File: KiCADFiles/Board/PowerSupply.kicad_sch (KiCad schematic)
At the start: 30 parts, among them J3 Barrel_Jack_PTH, U2 LT1962-3.3, U3 LT1962-5, U8 LT1962

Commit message: chose all components
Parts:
- removed C7: 47uF, ~, symbol SuperAudioBoard-rescue:CP1
- added C7: 100u, Capacitor_THT:CP_Radial_D5.0mm_P2.00mm, symbol Device:C_Small_US
- C1, C10, C11, C12, C13, C16, C17, C2, C3, C4, C8: value 10uF -> 10u; footprint ~ -> PCM_SparkFun-Capacitor:C_0805_2012Metric; MPN (none) -> CL21A106KAYNNNG; Voltage (none) -> 25V
- C5, C6: footprint ~ -> PCM_SparkFun-Capacitor:C_0603_1608Metric; MPN (none) -> C0603C103K5RACTU
- D1, D2: footprint ~ -> LED_SMD:LED_0805_2012Metric; MPN (none) -> 599-0110-137F
- FB1, FB2: value 330R -> 330; footprint ~ -> Inductor_SMD:L_0805_2012Metric; MPN (none) -> MPZ2012S331ATD25
- L2, L3: value 5.2uH -> 6.8uH; footprint ~ -> Inductor_SMD:L_0805_2012Metric; MPN (none) -> MLZ2012N6R8LT000
- R1: value 270 -> 3.3k; footprint ~ -> PCM_SparkFun-Resistor:R_0805_2012Metric; MPN (none) -> ERA-6AEB332V
- R2: value 620 -> 3.3k; footprint ~ -> PCM_SparkFun-Resistor:R_0805_2012Metric; MPN (none) -> ERA-6AEB332V
- R3: footprint (none) -> PCM_SparkFun-Resistor:R_0805_2012Metric; MPN (none) -> ERA-6AEB3922V; Tol (none) -> 1%
- R4: footprint (none) -> PCM_SparkFun-Resistor:R_0805_2012Metric; MPN (none) -> ERA-6AEB332V; Tol (none) -> 1%
- TP1, TP2: footprint (none) -> TestPoint:TestPoint_2Pads_Pitch2.54mm_Drill0.8mm; now not fitted
- U2: footprint (none) -> Package_SO:MSOP-8_3x3mm_P0.65mm; MPN (none) -> LT1962EMS8-3.3
- U3: footprint (none) -> Package_SO:MSOP-8_3x3mm_P0.65mm; MPN (none) -> LT1962EMS8-5
- U8: MPN (none) -> LT1962EMS8
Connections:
- net GND: now also C7.2
- net at C8.1, FB1.2, U8.5 (~{SHDN})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: now also C7.1

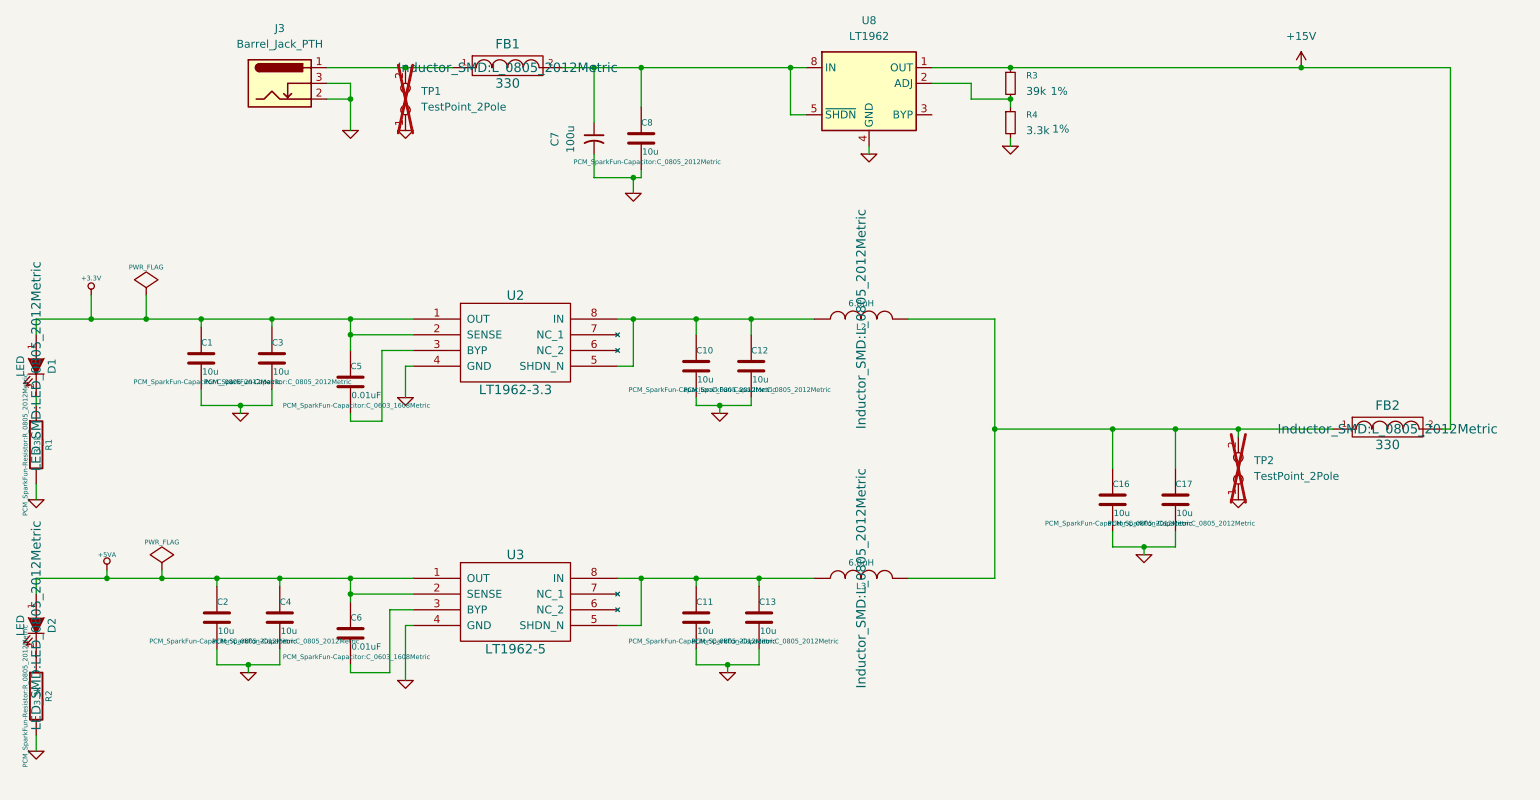
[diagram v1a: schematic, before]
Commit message: replaced sw with relay, routed line amp section
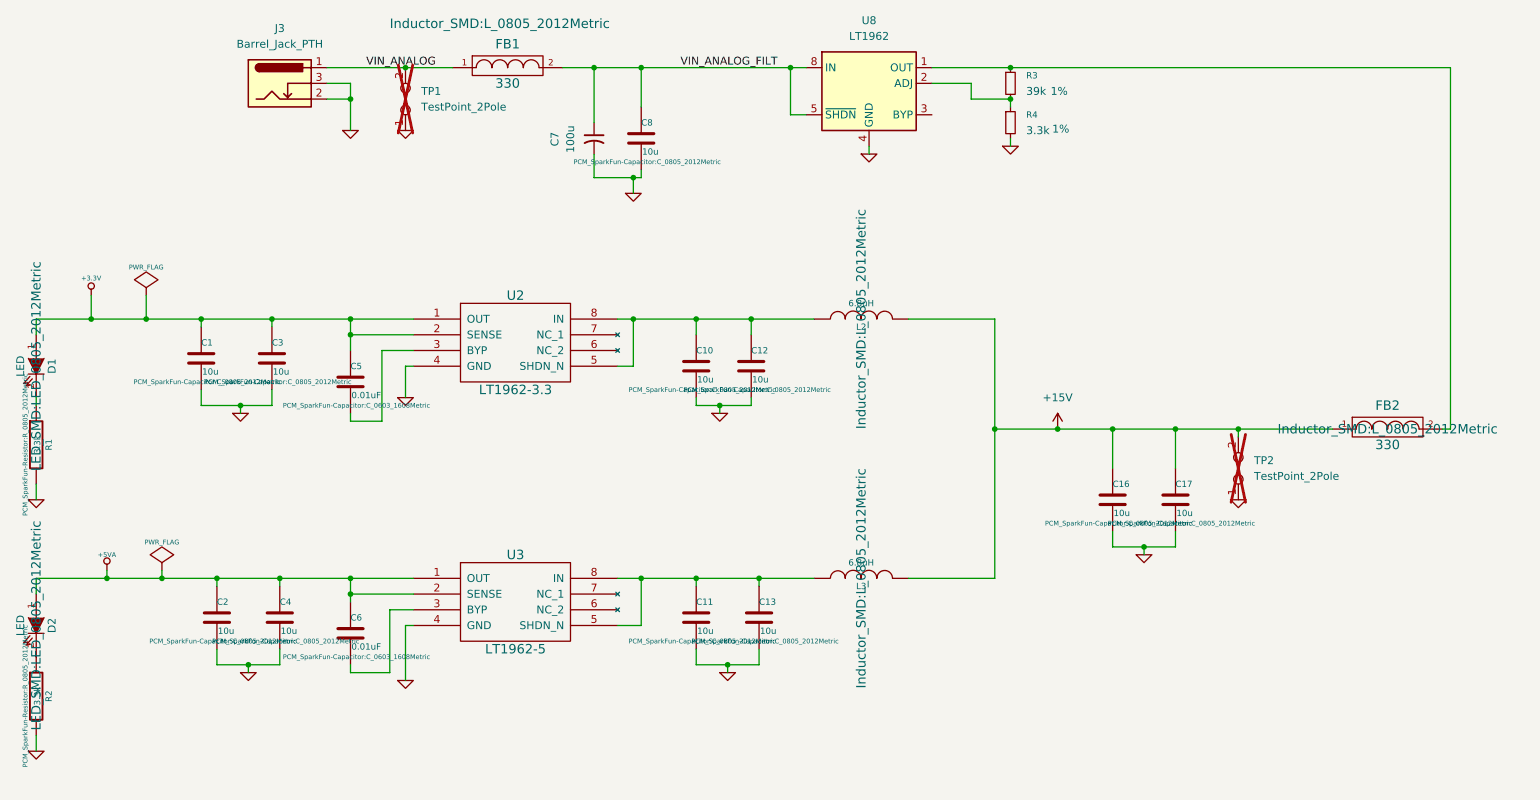
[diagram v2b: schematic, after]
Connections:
- net +15V: now also C16.1, C17.1, FB2.1, L2.2, L3.2, TP2.2; no longer FB2.2, R3.1, U8.1 (OUT)
- net VIN_ANALOG_FILT: now reaches C7.1, C8.1, FB1.2, U8.5 (~{SHDN}), U8.8 (IN)
- net VIN_ANALOG: now reaches FB1.1, J3.1 (PWR), TP1.2
- new net: FB2.2, R3.1, U8.1 (OUT)
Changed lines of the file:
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@@
 	)
 	(junction
-		(at 240.03 55.88)
-		(diameter 0)
-		(color 0 0 0 0)
-	)
-	(junction
 		(at 64.77 138.43)
 		(diameter 0)
@@
 	)
 	(junction
+		(at 200.66 114.3)
+		(diameter 0)
+		(color 0 0 0 0)
+	)
+	(junction
 		(at 74.93 138.43)
 		(diameter 0)
@@
 	(wire
 		(pts
-			(xy 240.03 55.88) (xy 264.16 55.88)
+			(xy 193.04 55.88) (xy 264.16 55.88)
 		)
 		(stroke
@@
 	(wire
 		(pts
-			(xy 193.04 55.88) (xy 240.03 55.88)
-		)
-		(stroke
-			(width 0)
-			(type default)
-		)
-	)
-	(wire
-		(pts
 			(xy 129.54 96.52) (xy 132.08 96.52)
 		)
@@
 	(wire
 		(pts
-			(xy 190.5 114.3) (xy 209.55 114.3)
+			(xy 190.5 114.3) (xy 200.66 114.3)
 		)
 		(stroke
@@
 	(wire
 		(pts
+			(xy 200.66 114.3) (xy 209.55 114.3)
+		)
+		(stroke
+			(width 0)
+			(type default)
+		)
+	)
+	(wire
+		(pts
 			(xy 62.23 97.79) (xy 62.23 96.52)
 		)
@@
 		)
 	)
+	(label "VIN_ANALOG"
+		(at 88.9 55.88 0)
+		(effects
+			(font
+				(size 1.27 1.27)
+			)
+			(justify left bottom)
+		)
+	)
+	(label "VIN_ANALOG_FILT"
+		(at 139.7 55.88 0)
+		(effects
+			(font
+				(size 1.27 1.27)
+			)
+			(justify left bottom)
+		)
+	)
 	(symbol
 		(lib_name "LT1962-3.3_2")
@@
 		(on_board yes)
 		(dnp no)
+		(fields_autoplaced yes)
 		(property "Reference" "#PWR010"
 			(at 132.08 76.2 0)
@@
 		(on_board yes)
 		(dnp no)
+		(fields_autoplaced yes)
 		(property "Reference" "C8"
 			(at 133.35 64.77 0)
@@
 		)
 		(property "Footprint" "Inductor_SMD:L_0805_2012Metric"
-			(at 111.76 55.88 0)
+			(at 110.49 48.768 0)
 			(effects
 				(font
@@
 	(symbol
 		(lib_id "power:+15V")
-		(at 240.03 55.88 0)
+		(at 200.66 114.3 0)
 		(unit 1)
 		(exclude_from_sim no)
@@
 		(fields_autoplaced yes)
 		(property "Reference" "#PWR012"
-			(at 240.03 59.69 0)
+			(at 200.66 118.11 0)
 			(effects
 				(font
@@
 		)
 		(property "Value" "+15V"
-			(at 240.03 50.8 0)
+			(at 200.66 109.22 0)
 			(effects
 				(font
@@
 		)
 		(property "Footprint" ""
-			(at 240.03 55.88 0)
+			(at 200.66 114.3 0)
 			(effects
 				(font
@@
 		)
 		(property "Datasheet" ""
-			(at 240.03 55.88 0)
+			(at 200.66 114.3 0)
 			(effects
 				(font
@@
 		)
 		(property "Description" "Power symbol creates a global label with name \"+15V\""
-			(at 240.03 55.88 0)
+			(at 200.66 114.3 0)
 			(effects
 				(font
@@
 		)
 		(instances
-			(project ""
+			(project "SuperAudioBoard"
 				(path "/01f65e03-4e05-4001-87b4-b3e88e4198ab/00000000-0000-0000-0000-000054459109"
 					(reference "#PWR012")
@@
 		(on_board yes)
 		(dnp no)
+		(fields_autoplaced yes)
 		(property "Reference" "R3"
 			(at 195.58 57.1499 0)
@@
 		(on_board yes)
 		(dnp no)
+		(fields_autoplaced yes)
 		(property "Reference" "C7"
 			(at 119.38 67.437 90)
@@
 		(on_board yes)
 		(dnp no)
+		(fields_autoplaced yes)
 		(property "Reference" "R4"
 			(at 195.58 63.4999 0)
@@
 		(on_board yes)
 		(dnp no)
+		(fields_autoplaced yes)
 		(property "Reference" "#PWR05"
 			(at 170.18 69.85 0)
@@
 		(on_board yes)
 		(dnp no)
+		(fields_autoplaced yes)
 		(property "Reference" "#PWR011"
 			(at 193.04 68.58 0)

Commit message: finished layout, passed DRC
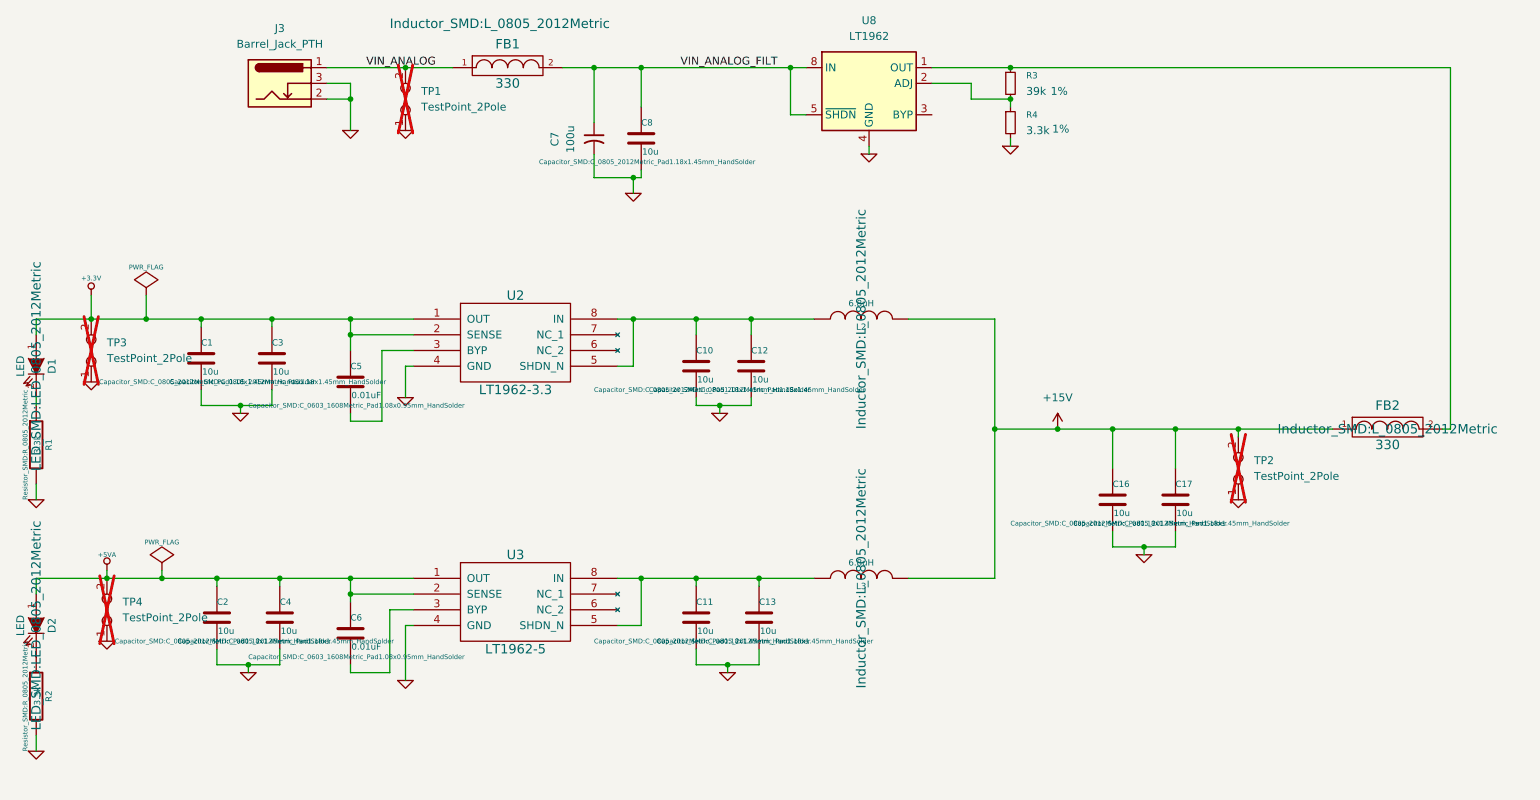
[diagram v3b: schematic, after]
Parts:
- added TP3, TP4: TestPoint_2Pole, TestPoint:TestPoint_2Pads_Pitch2.54mm_Drill0.8mm, symbol Connector:TestPoint_2Pole
- C1, C10, C11, C12, C13, C16, C17, C2, C3, C4, C8: footprint PCM_SparkFun-Capacitor:C_0805_2012Metric -> Capacitor_SMD:C_0805_2012Metric_Pad1.18x1.45mm_HandSolder
- C5, C6: footprint PCM_SparkFun-Capacitor:C_0603_1608Metric -> Capacitor_SMD:C_0603_1608Metric_Pad1.08x0.95mm_HandSolder
- R1, R2, R3, R4: footprint PCM_SparkFun-Resistor:R_0805_2012Metric -> Resistor_SMD:R_0805_2012Metric
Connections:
- net +3.3V: now also TP3.2
- net +5VA: now also TP4.2
- net GND: now also TP3.1, TP4.1
